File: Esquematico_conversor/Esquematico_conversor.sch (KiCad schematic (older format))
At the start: 23 parts, among them U1 4070

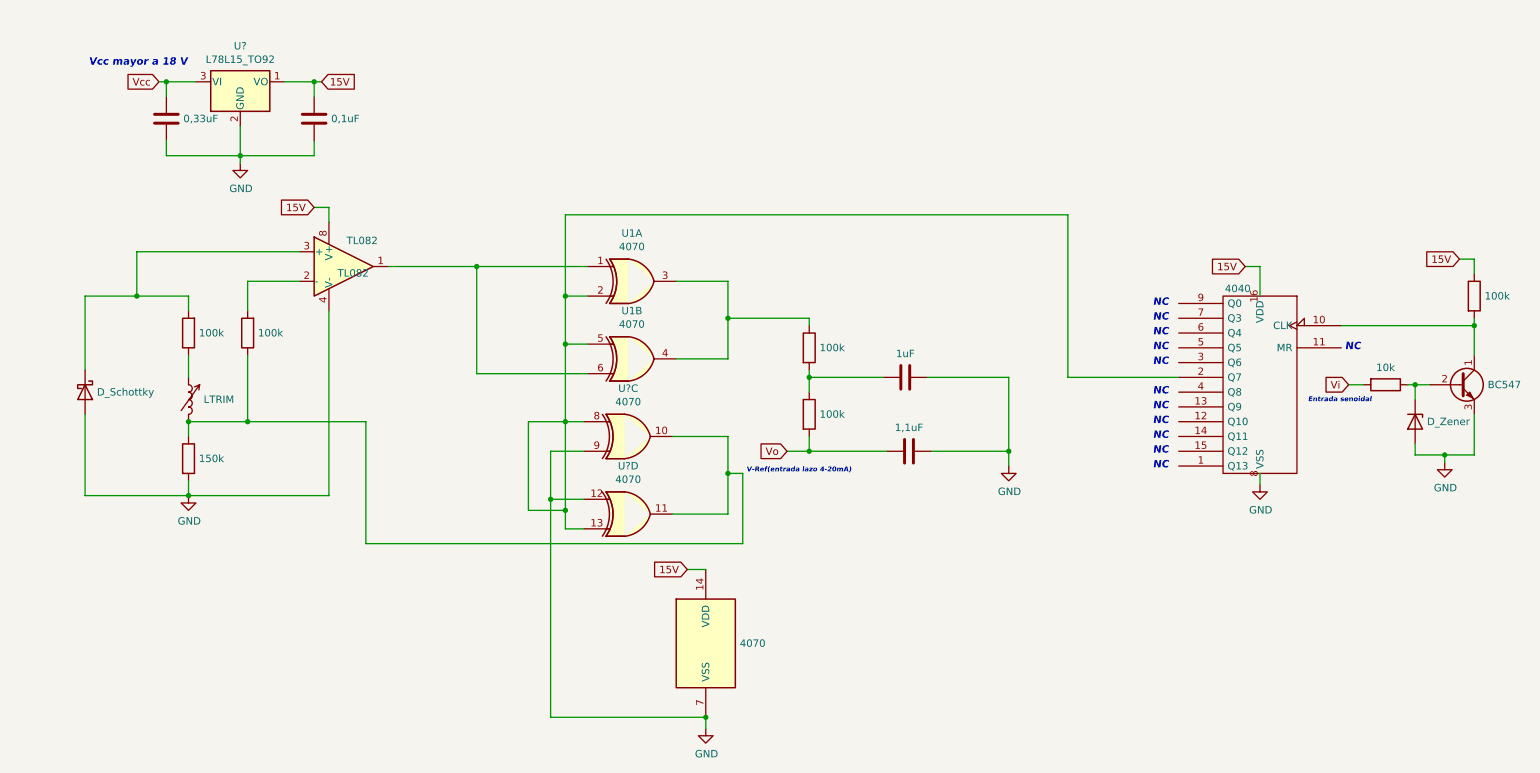
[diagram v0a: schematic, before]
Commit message: Referencias y valores de componentes del conversor
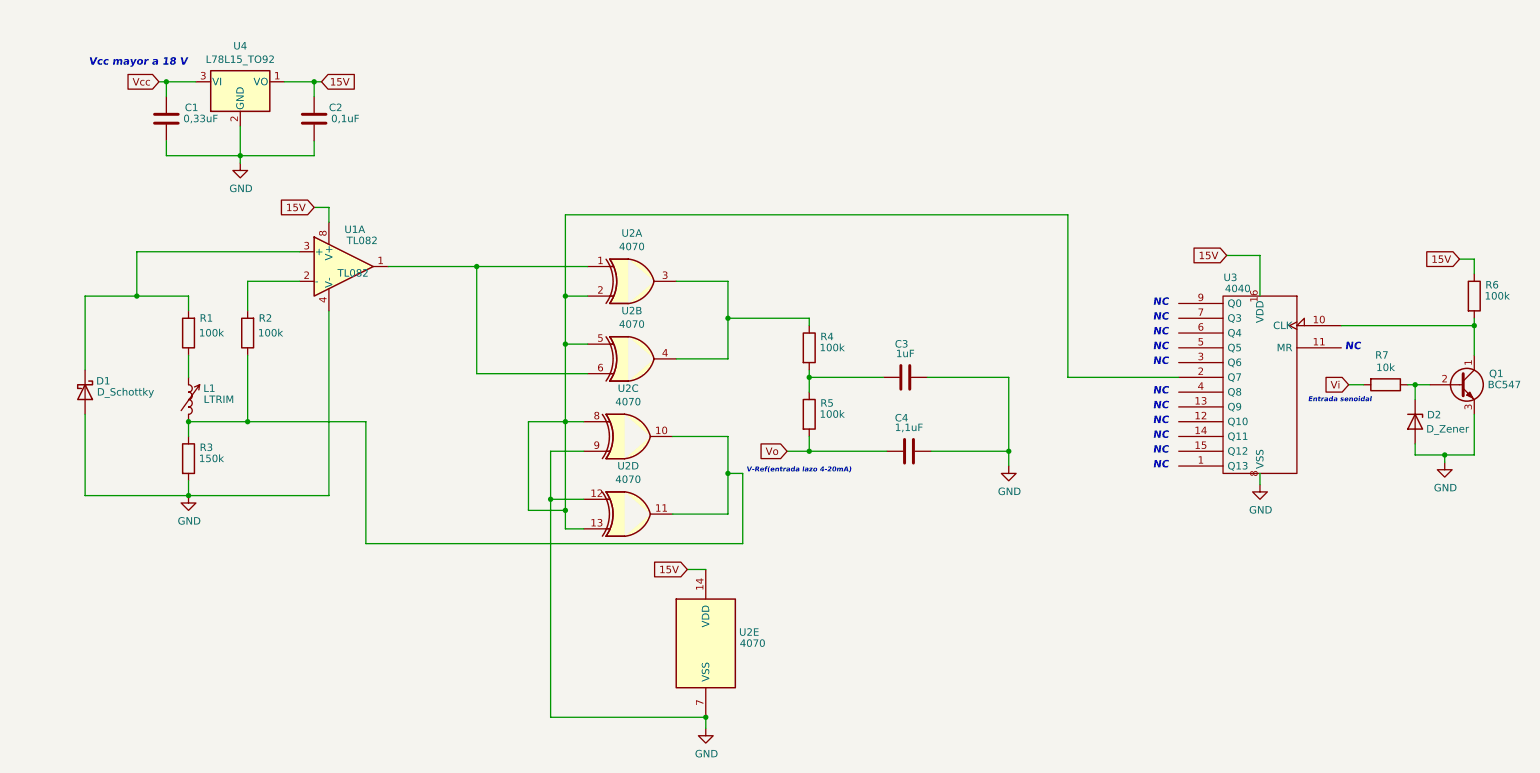
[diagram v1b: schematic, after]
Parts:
- gave numbers to parts that had none: 19
- renumbered U1 to U2

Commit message: Conversor frec/tension
Falta el footprint del sensor inductivo que no lo encontré y me tira 2 errores a las salidas del 4070...
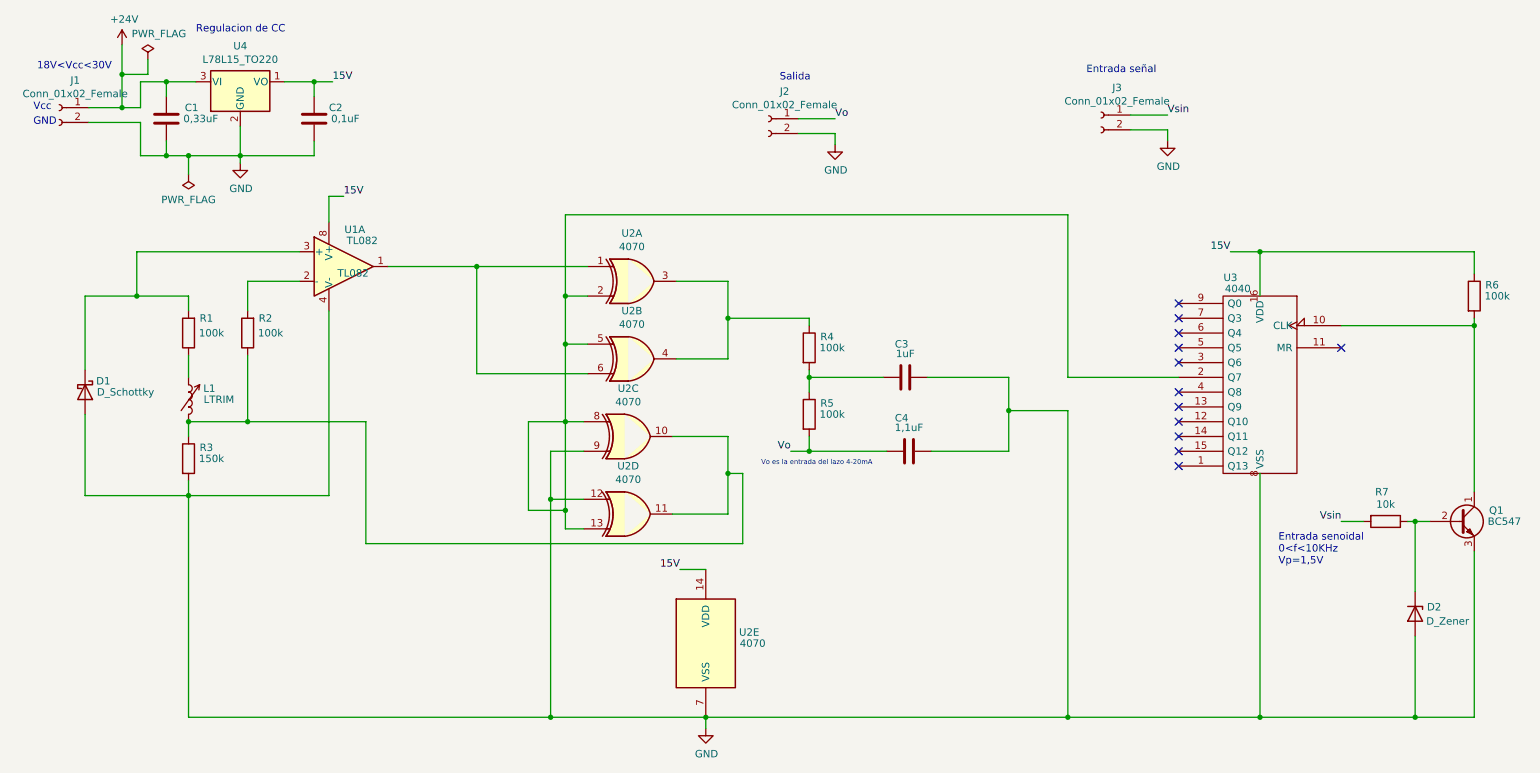
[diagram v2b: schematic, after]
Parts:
- added J1, J2, J3: Conn_01x02_Female, TerminalBlock:TerminalBlock_bornier-2_P5.08mm, symbol Connector:Conn_01x02_Female
- C1, C2, C3, C4: footprint (none) -> Capacitor_THT:CP_Radial_D6.3mm_P2.50mm
- D1: footprint (none) -> Diode_THT:D_DO-41_SOD81_P10.16mm_Horizontal
- D2: footprint (none) -> Diode_THT:D_DO-35_SOD27_P7.62mm_Horizontal
- R1, R2, R3, R4, R5, R6, R7: footprint (none) -> Resistor_THT:R_Axial_DIN0204_L3.6mm_D1.6mm_P7.62mm_Horizontal
- U1: footprint (none) -> Package_DIP:DIP-8_W7.62mm_LongPads
- U1: renamed from U?; footprint (none) -> Package_DIP:DIP-8_W7.62mm_LongPads
- U2: footprint (none) -> Package_DIP:DIP-14_W7.62mm_Socket_LongPads
- U3: footprint (none) -> Package_DIP:DIP-16_W7.62mm_LongPads
- U4: value L78L15_TO92 -> L78L15_TO220; footprint Package_TO_SOT_THT:TO-92_Inline -> Package_TO_SOT_THT:TO-220-3_Vertical
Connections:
- net GND: now also J1.2 (Pin_2), J2.2 (Pin_2), J3.2 (Pin_2)
- net Vo: now also J2.1 (Pin_1)
- net Vcc renamed +24V
- net +24V: now also J1.1 (Pin_1)
- net Vi renamed Vsin
- net Vsin: now also J3.1 (Pin_1)
- no-connect marks 0 -> 12
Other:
- note added: "18V<Vcc<30V\n"
- note added: "Entrada senoidal\n0<f<10KHz\nVp=1,5V"
- note added: "Entrada señal"
- note added: "GND"
- note added: "Regulacion de CC"
- note added: "Salida"
- note added: "Vcc"
- note added: "Vo es la entrada del lazo 4-20mA"
- note removed: "Entrada senoidal"
- note removed: "NC"
- note removed: "V-Ref(entrada lazo 4-20mA)"
- note removed: "Vcc mayor a 18 V\n"
- moved on the sheet: D2, Q1, R7
